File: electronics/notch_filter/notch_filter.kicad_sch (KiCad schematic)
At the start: 39 parts, among them J1 Conn_01x03, J2 Conn_01x03, J3 Output, J4 In, J5 module_2x15_left_input, J6 module_2x15_right_input, U1 opamp_single_8pin

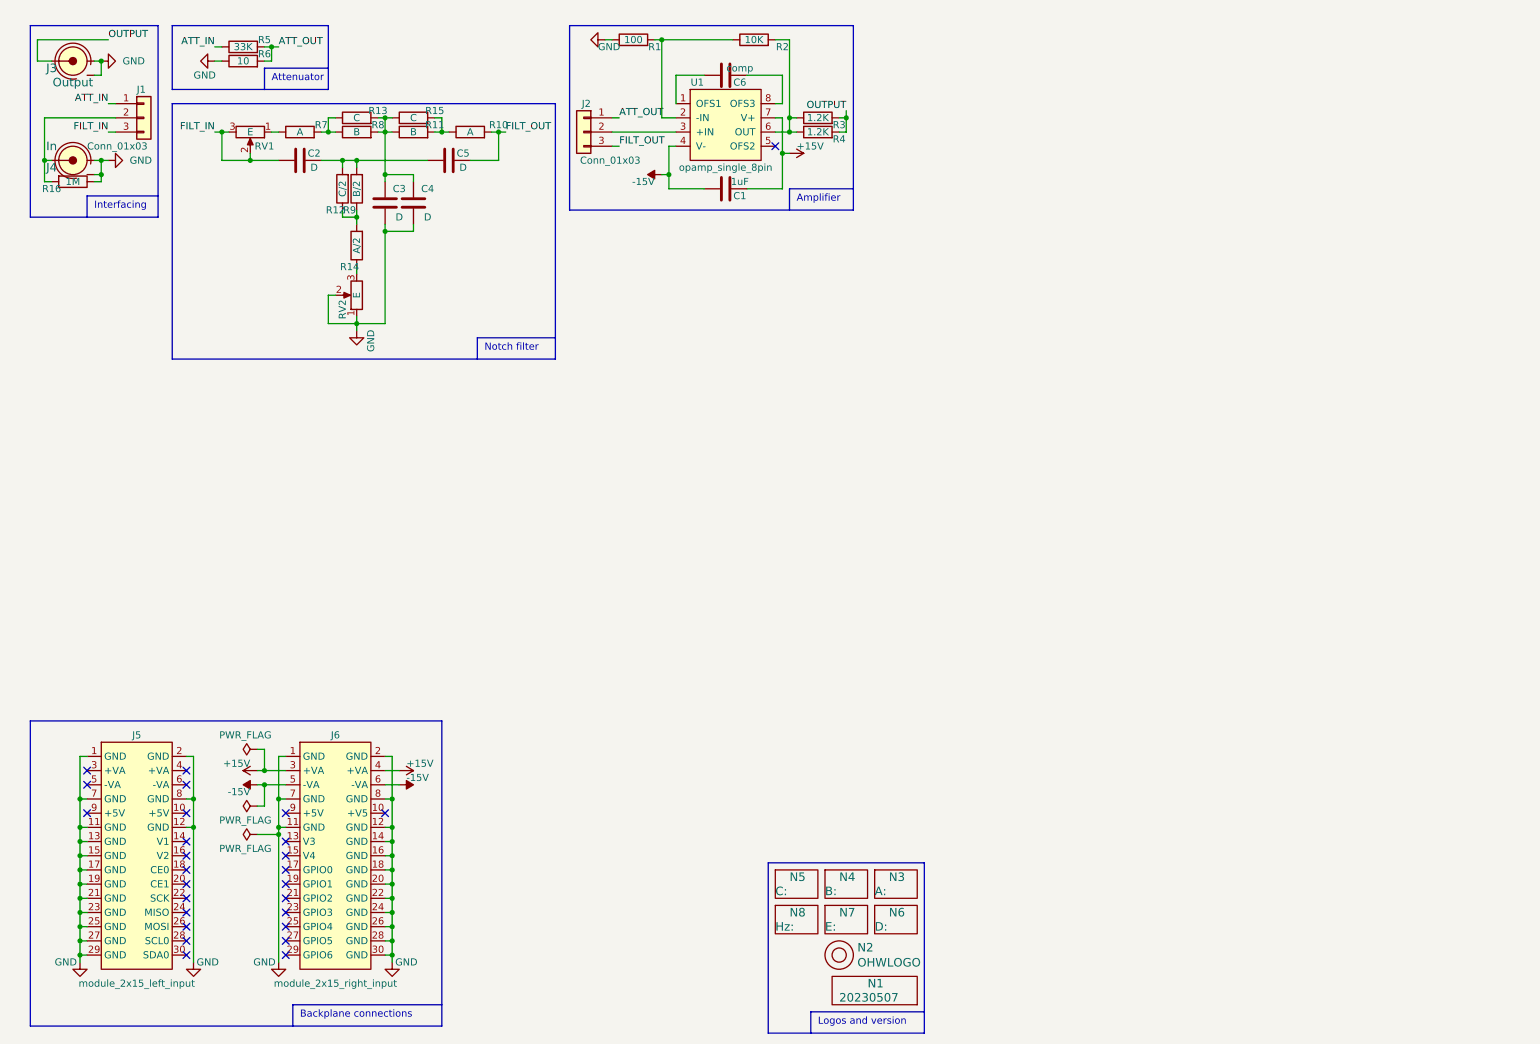
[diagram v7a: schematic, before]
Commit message: updated notch filter
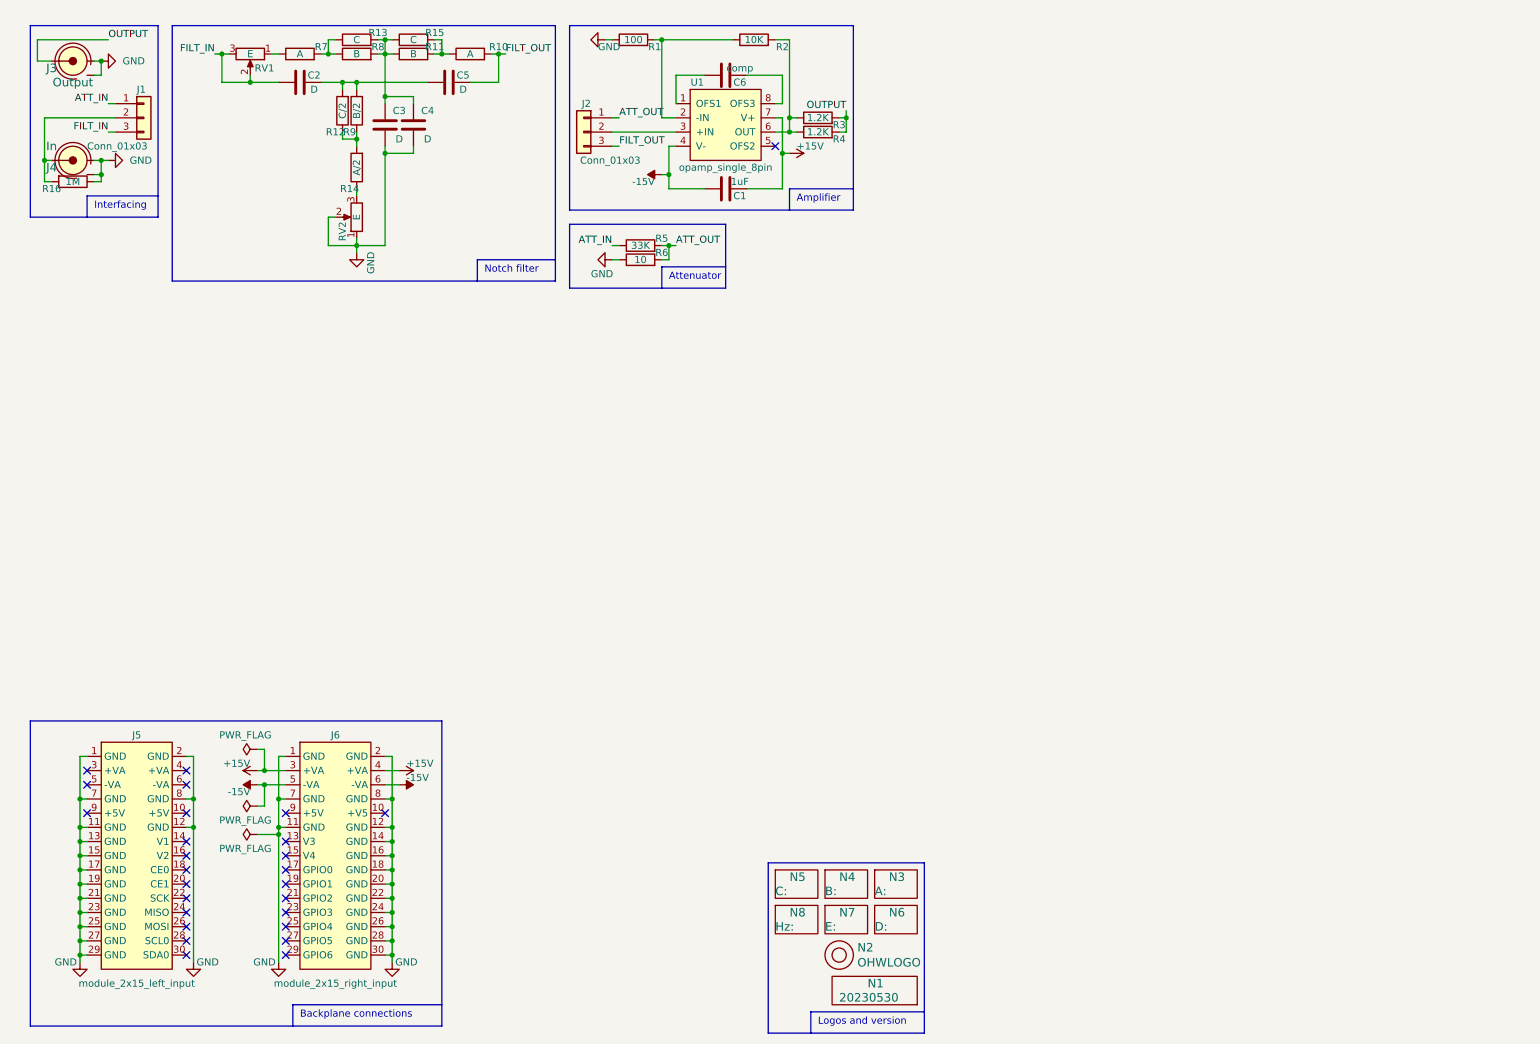
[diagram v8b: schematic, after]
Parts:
- C2, C3, C4, C5: footprint SquantorRcl:C-025_050-050X100-0805-3516-film -> SquantorRcl:C-050-050X100-0805-3516-film
- N1: value 20230507 -> 20230530
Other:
- moved on the sheet: C2, C3, C4, C5, R10, R11, R12, R13, R14, R15, R5, R6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
